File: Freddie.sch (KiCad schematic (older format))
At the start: 14 parts, among them J100 cond, J101 cond, U18 74LS08, U6 Freddie, Y1 Crystal

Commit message: GTIA
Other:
- moved on the sheet: R19, R20, U18A
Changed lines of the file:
@@
 $Descr A4 11693 8268
 encoding utf-8
-Sheet 5 13
+Sheet 5 14
 Title ""
 Date ""
@@
 L 74xx:74LS08 U18
 U 1 1 60220D8B
-P 8900 3025
-F 0 "U18" H 8900 3350 50  0000 C CNN
-F 1 "74LS08" H 8900 3259 50  0000 C CNN
-F 2 "Package_DIP:DIP-14_W7.62mm_Socket" H 8900 3025 50  0001 C CNN
-F 3 "http://www.ti.com/lit/gpn/sn74LS08" H 8900 3025 50  0001 C CNN
-	1    8900 3025
+P 8950 2800
+F 0 "U18" H 8950 3125 50  0000 C CNN
+F 1 "74LS08" H 8950 3034 50  0000 C CNN
+F 2 "Package_DIP:DIP-14_W7.62mm_Socket" H 8950 2800 50  0001 C CNN
+F 3 "http://www.ti.com/lit/gpn/sn74LS08" H 8950 2800 50  0001 C CNN
+	1    8950 2800
 	1    0    0    -1
 $EndComp
@@
 L Device:R R19
 U 1 1 602255FA
-P 8300 3125
-F 0 "R19" V 8300 3125 50  0000 C CNN
-F 1 "3k" V 8375 3125 50  0000 C CNN
-F 2 "Atari:R_Axial_DIN0207_L3.6mm_D2.2mm_P10.16mm_Horizontal" V 8230 3125 50  0001 C CNN
-F 3 "~" H 8300 3125 50  0001 C CNN
-	1    8300 3125
+P 8350 2900
+F 0 "R19" V 8350 2900 50  0000 C CNN
+F 1 "3k" V 8425 2900 50  0000 C CNN
+F 2 "Atari:R_Axial_DIN0207_L3.6mm_D2.2mm_P10.16mm_Horizontal" V 8280 2900 50  0001 C CNN
+F 3 "~" H 8350 2900 50  0001 C CNN
+	1    8350 2900
 	0    1    1    0
 $EndComp
@@
 L Device:R R20
 U 1 1 60225F1A
-P 8300 2925
-F 0 "R20" V 8300 2925 50  0000 C CNN
-F 1 "3k" V 8225 2925 50  0000 C CNN
-F 2 "Atari:R_Axial_DIN0207_L3.6mm_D2.2mm_P10.16mm_Horizontal" V 8230 2925 50  0001 C CNN
-F 3 "~" H 8300 2925 50  0001 C CNN
-	1    8300 2925
-	0    1    1    0
-$EndComp
-Wire Wire Line
-	8450 2925 8525 2925
-Text GLabel 9200 3025 2    50   Input ~ 0
+P 8350 2700
+F 0 "R20" V 8350 2700 50  0000 C CNN
+F 1 "3k" V 8275 2700 50  0000 C CNN
+F 2 "Atari:R_Axial_DIN0207_L3.6mm_D2.2mm_P10.16mm_Horizontal" V 8280 2700 50  0001 C CNN
+F 3 "~" H 8350 2700 50  0001 C CNN
+	1    8350 2700
+	0    1    1    0
+$EndComp
+Wire Wire Line
+	8500 2700 8575 2700
+Text GLabel 9250 2800 2    50   Input ~ 0
 BO2
 Wire Wire Line
-	8150 3125 8150 2925
+	8200 2900 8200 2700
 $Comp
 L power:+5VA #PWR0142
 U 1 1 602274F9
-P 8150 2450
-F 0 "#PWR0142" H 8150 2300 50  0001 C CNN
-F 1 "+5VA" H 8165 2623 50  0000 C CNN
-F 2 "" H 8150 2450 50  0001 C CNN
-F 3 "" H 8150 2450 50  0001 C CNN
-	1    8150 2450
-	1    0    0    -1
-$EndComp
-Wire Wire Line
-	8150 2450 8150 2925
-Connection ~ 8150 2925
-Text GLabel 8525 2750 1    50   Input ~ 0
+P 8200 2225
+F 0 "#PWR0142" H 8200 2075 50  0001 C CNN
+F 1 "+5VA" H 8215 2398 50  0000 C CNN
+F 2 "" H 8200 2225 50  0001 C CNN
+F 3 "" H 8200 2225 50  0001 C CNN
+	1    8200 2225
+	1    0    0    -1
+$EndComp
+Wire Wire Line
+	8200 2225 8200 2700
+Connection ~ 8200 2700
+Text GLabel 8575 2525 1    50   Input ~ 0
 O2
 Wire Wire Line
-	8450 3125 8600 3125
-Wire Wire Line
-	8525 2750 8525 2925
-Connection ~ 8525 2925
-Wire Wire Line
-	8525 2925 8600 2925
+	8500 2900 8650 2900
+Wire Wire Line
+	8575 2525 8575 2700
+Connection ~ 8575 2700
+Wire Wire Line
+	8575 2700 8650 2700
 $Comp
 L Connector_Generic:Conn_01x01 J100

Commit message: Schema finished
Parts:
- added C43: 100nF, Atari:C_Axial_L5.1mm_D2.5mm_P12.50mm_Horizontal, symbol Device:C
- added unit 5 of U18
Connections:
- net +5VA: now also C43.1, U18.14 (VCC)
- net GND: now also C43.2, U18.7 (GND)
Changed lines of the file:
@@
 	4200 1825 4200 2575
 Connection ~ 2950 1825
+$Comp
+L 74xx:74LS08 U18
+U 5 1 603127C5
+P 10275 2725
+F 0 "U18" H 10505 2771 50  0000 L CNN
+F 1 "74LS08" H 10505 2680 50  0000 L CNN
+F 2 "Package_DIP:DIP-14_W7.62mm_Socket" H 10275 2725 50  0001 C CNN
+F 3 "http://www.ti.com/lit/gpn/sn74LS08" H 10275 2725 50  0001 C CNN
+	5    10275 2725
+	1    0    0    -1
+$EndComp
+$Comp
+L power:+5VA #PWR0235
+U 1 1 60314A8A
+P 10275 2125
+F 0 "#PWR0235" H 10275 1975 50  0001 C CNN
+F 1 "+5VA" H 10290 2298 50  0000 C CNN
+F 2 "" H 10275 2125 50  0001 C CNN
+F 3 "" H 10275 2125 50  0001 C CNN
+	1    10275 2125
+	1    0    0    -1
+$EndComp
+Wire Wire Line
+	10275 2125 10275 2225
+$Comp
+L power:GND #PWR0236
+U 1 1 6031559C
+P 10275 3325
+F 0 "#PWR0236" H 10275 3075 50  0001 C CNN
+F 1 "GND" H 10280 3152 50  0000 C CNN
+F 2 "" H 10275 3325 50  0001 C CNN
+F 3 "" H 10275 3325 50  0001 C CNN
+	1    10275 3325
+	1    0    0    -1
+$EndComp
+Wire Wire Line
+	10275 3225 10275 3325
+$Comp
+L Device:C C43
+U 1 1 603176DF
+P 10900 2700
+F 0 "C43" H 10925 2800 50  0000 L CNN
+F 1 "100nF" H 10925 2600 50  0000 L CNN
+F 2 "Atari:C_Axial_L5.1mm_D2.5mm_P12.50mm_Horizontal" H 10938 2550 50  0001 C CNN
+F 3 "~" H 10900 2700 50  0001 C CNN
+	1    10900 2700
+	1    0    0    -1
+$EndComp
+Wire Wire Line
+	10275 2225 10900 2225
+Wire Wire Line
+	10900 2225 10900 2550
+Connection ~ 10275 2225
+Wire Wire Line
+	10275 3225 10900 3225
+Wire Wire Line
+	10900 3225 10900 2850
+Connection ~ 10275 3225
 $EndSCHEMATC

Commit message: Tracking
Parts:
- R18, R26: footprint Atari:R_Axial_DIN0207_L3.6mm_D2.2mm_P10.16mm_Horizontal -> Resistor_THT:R_Axial_DIN0207_L6.3mm_D2.5mm_P10.16mm_Horizontal
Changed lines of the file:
@@
 F 0 "R18" V 3843 1825 50  0000 C CNN
 F 1 "240" V 3934 1825 50  0000 C CNN
-F 2 "Atari:R_Axial_DIN0207_L3.6mm_D2.2mm_P10.16mm_Horizontal" V 3980 1825 50  0001 C CNN
+F 2 "Resistor_THT:R_Axial_DIN0207_L6.3mm_D2.5mm_P10.16mm_Horizontal" V 3980 1825 50  0001 C CNN
 F 3 "~" H 4050 1825 50  0001 C CNN
 	1    4050 1825
@@
 F 0 "R26" V 3843 2575 50  0000 C CNN
 F 1 "1M" V 3934 2575 50  0000 C CNN
-F 2 "Atari:R_Axial_DIN0207_L3.6mm_D2.2mm_P10.16mm_Horizontal" V 3980 2575 50  0001 C CNN
+F 2 "Resistor_THT:R_Axial_DIN0207_L6.3mm_D2.5mm_P10.16mm_Horizontal" V 3980 2575 50  0001 C CNN
 F 3 "~" H 4050 2575 50  0001 C CNN
 	1    4050 2575

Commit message: Trackimg
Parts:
- added J200: Diagnostic Signal, Connector_PinHeader_2.54mm:PinHeader_1x08_P2.54mm_Vertical, symbol Connector_Generic:Conn_01x08
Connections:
- net CAS: now also J200.6 (Pin_6)
- net CASINH: now also J200.5 (Pin_5)
- net EXTSEL: now also J200.2 (Pin_2)
- net O2: now also J200.1 (Pin_1)
- net OSC: now also J200.4 (Pin_4)
- net RAS: now also J200.8 (Pin_8)
- net RW: now also J200.3 (Pin_3)
- net WRT: now also J200.7 (Pin_7)
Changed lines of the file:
@@
 	10900 3225 10900 2850
 Connection ~ 10275 3225
+$Comp
+L Connector_Generic:Conn_01x08 J200
+U 1 1 60415DC7
+P 8150 4025
+F 0 "J200" H 8230 4017 50  0000 L CNN
+F 1 "Diagnostic Signal" H 8230 3926 50  0000 L CNN
+F 2 "Connector_PinHeader_2.54mm:PinHeader_1x08_P2.54mm_Vertical" H 8150 4025 50  0001 C CNN
+F 3 "~" H 8150 4025 50  0001 C CNN
+	1    8150 4025
+	1    0    0    -1
+$EndComp
+Text GLabel 7950 4225 0    50   Input ~ 0
+CAS
+Text GLabel 7950 4325 0    50   Input ~ 0
+WRT
+Text GLabel 7950 4425 0    50   Input ~ 0
+RAS
+Text GLabel 7950 3925 0    50   Input ~ 0
+RW
+Text GLabel 7950 4025 0    50   Input ~ 0
+OSC
+Text GLabel 7950 3725 0    50   Input ~ 0
+O2
+Text GLabel 7950 4125 0    50   Input ~ 0
+CASINH
+Text GLabel 7950 3825 0    50   Input ~ 0
+EXTSEL
 $EndSCHEMATC

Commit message: Diagnostic
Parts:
- removed J200: Diagnostic Signal, Connector_PinHeader_2.54mm:PinHeader_1x08_P2.54mm_Vertical, symbol Connector_Generic:Conn_01x08
- added J200: Diag, Connector_PinHeader_2.54mm:PinHeader_1x10_P2.54mm_Vertical, symbol Connector_Generic:Conn_01x10
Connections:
- net CAS: now also J200.7 (Pin_7)
- net CASINH: now also J200.6 (Pin_6)
- net EXTSEL: now also J200.3 (Pin_3)
- net GND: now also J200.10 (Pin_10)
- net O2: now also J200.1 (Pin_1)
- net OSC: now also J200.5 (Pin_5)
- net RAS: now also J200.9 (Pin_9)
- net RW: now also J200.4 (Pin_4)
- net WRT: now also J200.8 (Pin_8)
- new net REF: J200.2 (Pin_2)
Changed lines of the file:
@@
 	10900 3225 10900 2850
 Connection ~ 10275 3225
-$Comp
-L Connector_Generic:Conn_01x08 J200
-U 1 1 60415DC7
-P 8150 4025
-F 0 "J200" H 8230 4017 50  0000 L CNN
-F 1 "Diagnostic Signal" H 8230 3926 50  0000 L CNN
-F 2 "Connector_PinHeader_2.54mm:PinHeader_1x08_P2.54mm_Vertical" H 8150 4025 50  0001 C CNN
-F 3 "~" H 8150 4025 50  0001 C CNN
-	1    8150 4025
-	1    0    0    -1
-$EndComp
-Text GLabel 7950 4225 0    50   Input ~ 0
+Text GLabel 7950 4325 0    50   Input ~ 0
 CAS
-Text GLabel 7950 4325 0    50   Input ~ 0
+Text GLabel 7950 4425 0    50   Input ~ 0
 WRT
-Text GLabel 7950 4425 0    50   Input ~ 0
+Text GLabel 7950 4525 0    50   Input ~ 0
 RAS
-Text GLabel 7950 3925 0    50   Input ~ 0
+Text GLabel 7950 4025 0    50   Input ~ 0
 RW
-Text GLabel 7950 4025 0    50   Input ~ 0
+Text GLabel 7950 4125 0    50   Input ~ 0
 OSC
 Text GLabel 7950 3725 0    50   Input ~ 0
 O2
-Text GLabel 7950 4125 0    50   Input ~ 0
+Text GLabel 7950 4225 0    50   Input ~ 0
 CASINH
+Text GLabel 7950 3925 0    50   Input ~ 0
+EXTSEL
+$Comp
+L Connector_Generic:Conn_01x10 J200
+U 1 1 60423A62
+P 8150 4125
+F 0 "J200" H 8230 4117 50  0000 L CNN
+F 1 "Diag" H 8230 4026 50  0000 L CNN
+F 2 "Connector_PinHeader_2.54mm:PinHeader_1x10_P2.54mm_Vertical" H 8150 4125 50  0001 C CNN
+F 3 "~" H 8150 4125 50  0001 C CNN
+	1    8150 4125
+	1    0    0    -1
+$EndComp
 Text GLabel 7950 3825 0    50   Input ~ 0
-EXTSEL
+REF
+Text GLabel 7950 4625 0    50   Input ~ 0
+GND
 $EndSCHEMATC

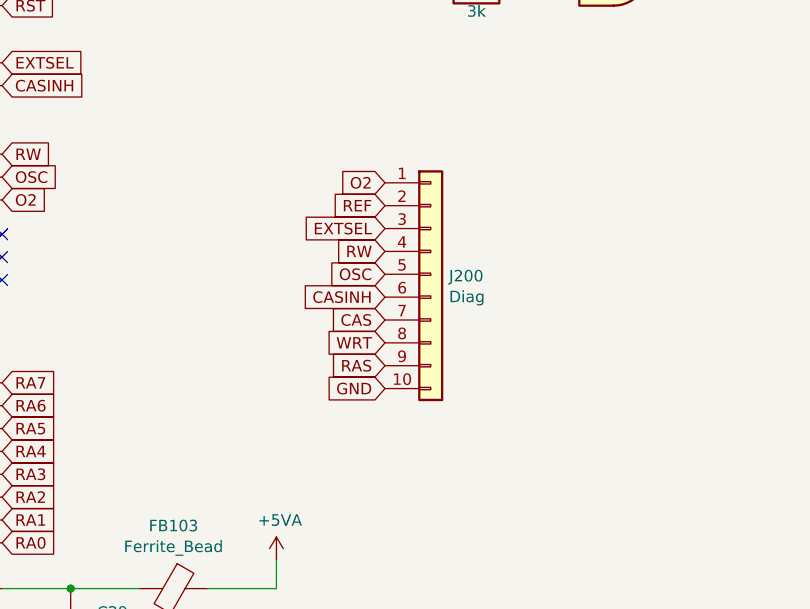
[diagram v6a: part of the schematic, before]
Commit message: Diagnostic pin
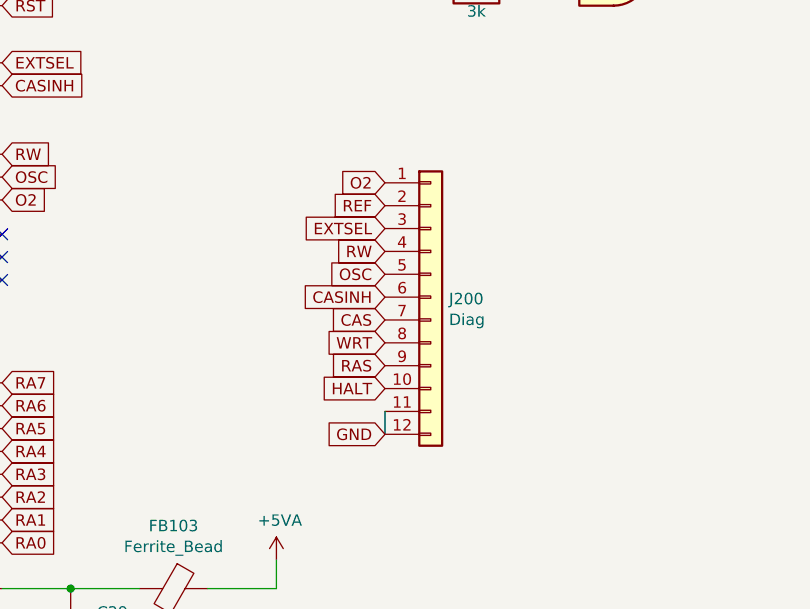
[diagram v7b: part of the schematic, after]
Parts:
- removed J200: Diag, Connector_PinHeader_2.54mm:PinHeader_1x10_P2.54mm_Vertical, symbol Connector_Generic:Conn_01x10
- added J200: Diag, Connector_PinHeader_2.54mm:PinHeader_1x12_P2.54mm_Vertical, symbol Connector_Generic:Conn_01x12
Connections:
- net CAS: now also J200.7 (Pin_7)
- net CASINH: now also J200.6 (Pin_6)
- net EXTSEL: now also J200.3 (Pin_3)
- net GND: now also J200.11 (Pin_11), J200.12 (Pin_12)
- net O2: now also J200.1 (Pin_1)
- net OSC: now also J200.5 (Pin_5)
- net RAS: now also J200.9 (Pin_9)
- net REF: now also J200.2 (Pin_2)
- net RW: now also J200.4 (Pin_4)
- net WRT: now also J200.8 (Pin_8)
- new net HALT: J200.10 (Pin_10)
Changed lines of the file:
@@
 Text GLabel 7950 3925 0    50   Input ~ 0
 EXTSEL
+Text GLabel 7950 3825 0    50   Input ~ 0
+REF
+Text GLabel 7950 4825 0    50   Input ~ 0
+GND
 $Comp
-L Connector_Generic:Conn_01x10 J200
-U 1 1 60423A62
-P 8150 4125
-F 0 "J200" H 8230 4117 50  0000 L CNN
-F 1 "Diag" H 8230 4026 50  0000 L CNN
-F 2 "Connector_PinHeader_2.54mm:PinHeader_1x10_P2.54mm_Vertical" H 8150 4125 50  0001 C CNN
-F 3 "~" H 8150 4125 50  0001 C CNN
-	1    8150 4125
+L Connector_Generic:Conn_01x12 J200
+U 1 1 6047EC37
+P 8150 4225
+F 0 "J200" H 8230 4217 50  0000 L CNN
+F 1 "Diag" H 8230 4126 50  0000 L CNN
+F 2 "Connector_PinHeader_2.54mm:PinHeader_1x12_P2.54mm_Vertical" H 8150 4225 50  0001 C CNN
+F 3 "~" H 8150 4225 50  0001 C CNN
+	1    8150 4225
 	1    0    0    -1
 $EndComp
-Text GLabel 7950 3825 0    50   Input ~ 0
-REF
 Text GLabel 7950 4625 0    50   Input ~ 0
-GND
+HALT
+Wire Wire Line
+	7950 4725 7950 4825
 $EndSCHEMATC

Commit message: Error remove
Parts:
- C32, C33: value 100nF -> 22pF
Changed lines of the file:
@@
 P 3325 1825
 F 0 "C32" V 3073 1825 50  0000 C CNN
-F 1 "100nF" V 3164 1825 50  0000 C CNN
+F 1 "22pF" V 3164 1825 50  0000 C CNN
 F 2 "Atari:C_Axial_L5.1mm_D2.5mm_P12.50mm_Horizontal" H 3363 1675 50  0001 C CNN
 F 3 "~" H 3325 1825 50  0001 C CNN
@@
 P 3325 2575
 F 0 "C33" V 3073 2575 50  0000 C CNN
-F 1 "100nF" V 3164 2575 50  0000 C CNN
+F 1 "22pF" V 3164 2575 50  0000 C CNN
 F 2 "Atari:C_Axial_L5.1mm_D2.5mm_P12.50mm_Horizontal" H 3363 2425 50  0001 C CNN
 F 3 "~" H 3325 2575 50  0001 C CNN
